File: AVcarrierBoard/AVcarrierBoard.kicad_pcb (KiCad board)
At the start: 4 copper layers, 253.6 x 59 mm, 18 parts, among them J1 Mech_Switch, J2 Mech_Switch, J3 MainRecov, J4 DrogRecov, J5 Staging, J6 Mech_Switch, U2 WiFi Switch, U3 EggtimerQuantum, U4 EggfinderMini/FeatherGPS, U5 Blue_Raven

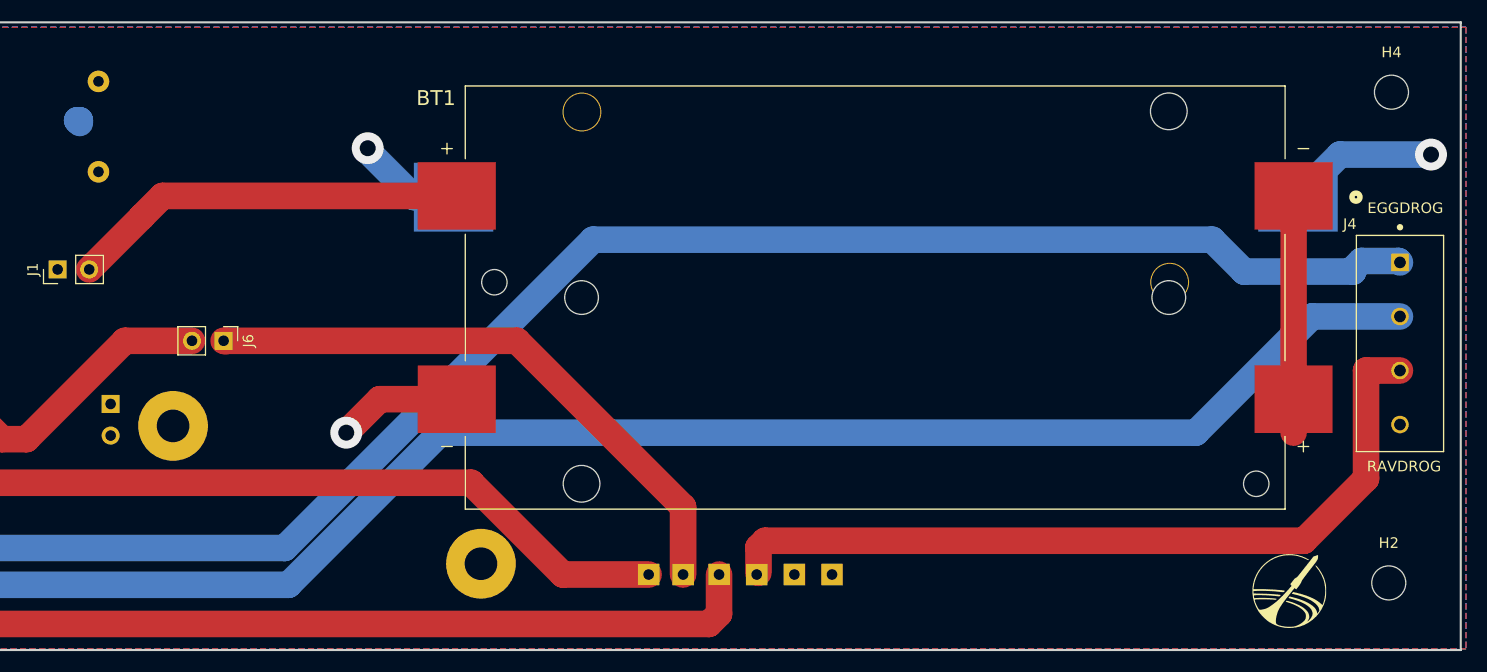
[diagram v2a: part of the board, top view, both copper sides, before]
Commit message: Added mounting holes for battery holders
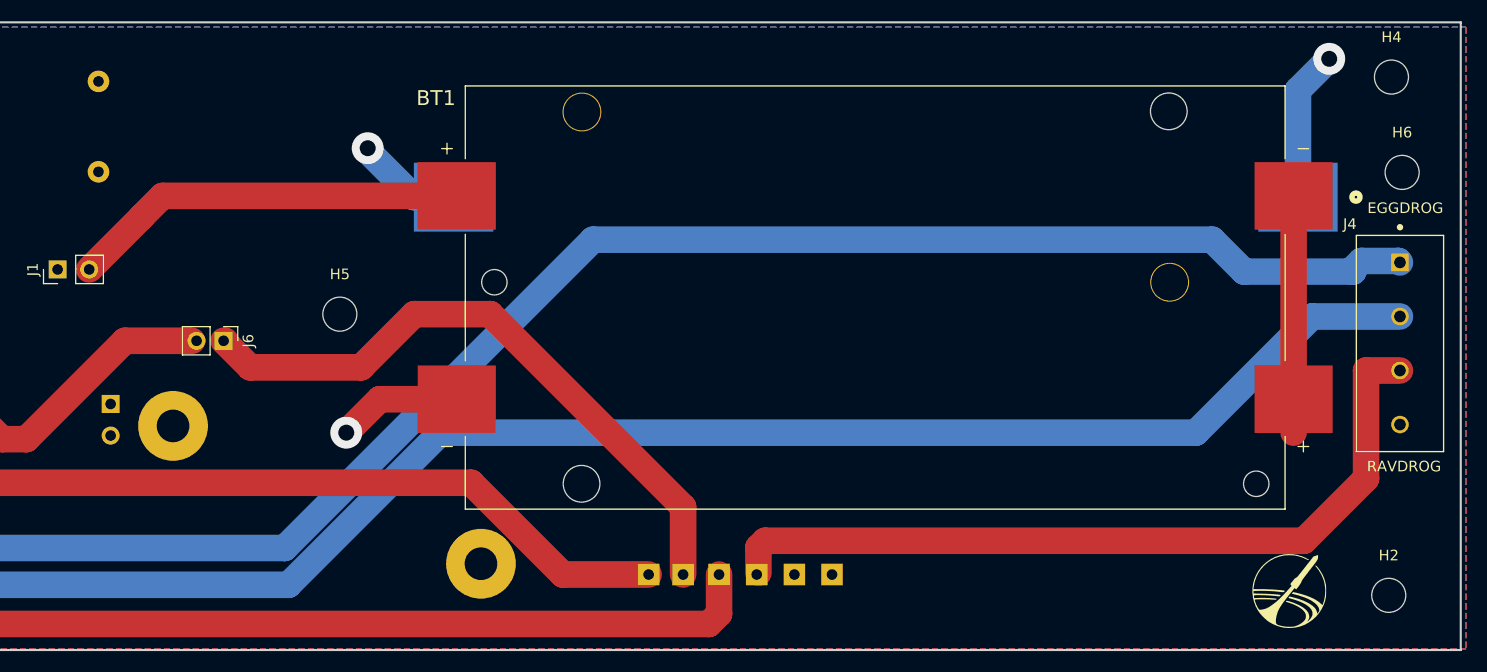
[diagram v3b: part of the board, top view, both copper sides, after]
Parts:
- added H5: M3, MountingHole:MountingHole_3.2mm_M3_ISO14580, F.Cu at (171.0, 93.0)
- added H6: M3, MountingHole:MountingHole_3.2mm_M3_ISO14580, F.Cu at (270.9, 79.7)
- J6: footprint 2.97mmSwitchConnector:PinHeader_1x02_P2.97mm_Vertical -> Connector_PinHeader_2.54mm:PinHeader_1x02_P2.54mm_Vertical
- moved H4 1.42 mm to (269.8, 70.7)
- moved H2 1.17 mm to (269.6, 119.4)
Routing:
- net +3V8: track 157.2 -> 151.4 mm
- net Raven3RD: track 56.1 -> 60.2 mm
- net GND2: track 10.9 -> 10.2 mm

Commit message: fix a bit
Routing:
- net +3V8: track 151.4 -> 129.8 mm
- net RavenMotIgnition: track 132.2 -> 124.5 mm
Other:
- board text added: "Phoenix 1.1"
- board text removed: "Phoenix 1.0"
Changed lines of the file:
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@@
   (gr_rect (start 22.765 65.57) (end 276.365 124.57)
     (stroke (width 0.2) (type default)) (fill none) (layer "Edge.Cuts"))
-  (gr_text "Phoenix 1.0\n" (at 265.7348 119.7864) (layer "B.SilkS")
+  (gr_text "Phoenix 1.1\n" (at 265.7348 119.7864) (layer "B.SilkS")
     (effects (font (size 3 3) (thickness 0.15)) (justify left bottom mirror))
   )
@@
     (effects (font (size 1 1) (thickness 0.15)) (justify right bottom))
   )
-  (via (at 264 69) (size 3) (drill 1.5) (layers "F.Cu" "B.Cu") (free) (net 1))
-  (segment (start 149.4536 104.4126) (end 149.4536 106.4768) (width 2.5) (layer "In1.Cu") (net 1))
-  (segment (start 149.4536 106.4768) (end 155.4988 112.522) (width 2.5) (layer "In1.Cu") (net 1))
-  (segment (start 219.9132 104.14) (end 243.2812 80.772) (width 2.5) (layer "In1.Cu") (net 1))
-  (segment (start 263 69) (end 264 69) (width 2.5) (layer "In1.Cu") (net 1))
-  (segment (start 155.4988 112.522) (end 171.958 112.522) (width 2.5) (layer "In1.Cu") (net 1))
-  (segment (start 243.2812 80.772) (end 251.228 80.772) (width 2.5) (layer "In1.Cu") (net 1))
-  (segment (start 251.228 80.772) (end 263 69) (width 2.5) (layer "In1.Cu") (net 1))
-  (segment (start 171.958 112.522) (end 180.34 104.14) (width 2.5) (layer "In1.Cu") (net 1))
-  (segment (start 180.34 104.14) (end 219.9132 104.14) (width 2.5) (layer "In1.Cu") (net 1))
-  (segment (start 261.065 81.999) (end 261.065 71.935) (width 2.5) (layer "B.Cu") (net 1))
-  (segment (start 261.065 71.935) (end 264 69) (width 2.5) (layer "B.Cu") (net 1))
+  (via (at 251.228 80.772) (size 3) (drill 1.5) (layers "F.Cu" "B.Cu") (free) (net 1))
+  (segment (start 155.4988 112.522) (end 149.4536 106.4768) (width 2.5) (layer "In1.Cu") (net 1))
+  (segment (start 171.958 112.522) (end 155.4988 112.522) (width 2.5) (layer "In1.Cu") (net 1))
+  (segment (start 243.2812 80.772) (end 219.9132 104.14) (width 2.5) (layer "In1.Cu") (net 1))
+  (segment (start 251.228 80.772) (end 243.2812 80.772) (width 2.5) (layer "In1.Cu") (net 1))
+  (segment (start 180.34 104.14) (end 171.958 112.522) (width 2.5) (layer "In1.Cu") (net 1))
+  (segment (start 219.9132 104.14) (end 180.34 104.14) (width 2.5) (layer "In1.Cu") (net 1))
+  (segment (start 149.4536 106.4768) (end 149.4536 104.4126) (width 2.5) (layer "In1.Cu") (net 1))
+  (segment (start 251.228 80.772) (end 259.838 80.772) (width 2.5) (layer "B.Cu") (net 1))
+  (segment (start 259.838 80.772) (end 261.065 81.999) (width 2.5) (layer "B.Cu") (net 1))
   (segment (start 174.7474 100.995) (end 181.99 100.995) (width 2.5) (layer "F.Cu") (net 2))
   (segment (start 172.2074 103.535) (end 174.7474 100.995) (width 2.5) (layer "F.Cu") (net 2))
@@
   (segment (start 182 82) (end 177.9614 82) (width 2.5) (layer "B.Cu") (net 14))
   (segment (start 177.9614 82) (end 173.618 77.6566) (width 2.5) (layer "B.Cu") (net 14))
-  (segment (start 150.7922 95.504) (end 157.1008 95.504) (width 2.5) (layer "F.Cu") (net 15))
-  (segment (start 141.5466 104.7496) (end 150.7922 95.504) (width 2.5) (layer "F.Cu") (net 15))
-  (segment (start 139.2428 104.7496) (end 141.5466 104.7496) (width 2.5) (layer "F.Cu") (net 15))
-  (segment (start 127.2032 92.71) (end 139.2428 104.7496) (width 2.5) (layer "F.Cu") (net 15))
+  (segment (start 127.2032 92.71) (end 129.9972 95.504) (width 2.5) (layer "F.Cu") (net 15))
+  (segment (start 129.9972 95.504) (end 157.1008 95.504) (width 2.5) (layer "F.Cu") (net 15))
   (via (at 127.2032 92.71) (size 3) (drill 2) (layers "F.Cu" "B.Cu") (net 15))
   (segment (start 43.557799 86.130432) (end 39.3578 81.930433) (width 2.5) (layer "B.Cu") (net 15))

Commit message: changes to blue raven orientation, radio power, wifi gnd, etc.
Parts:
- J1, J2: footprint 2.97mmSwitchConnector:PinHeader_1x02_P2.97mm_Vertical -> COTS_Boards:CON_436500227_MOL
- J6: footprint Connector_PinHeader_2.54mm:PinHeader_1x02_P2.54mm_Vertical -> COTS_Boards:CON_436500227_MOL
- moved U5 50.0 mm to (198.2, 101.3), turned to 180 degrees
- moved J6 24.6 mm to (156.2, 71.2), turned to 180 degrees
- moved J2 21.5 mm to (156.5, 81.1)
- moved J1 15.1 mm to (159.4, 91.4), turned to 0 degrees
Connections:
- U2 pad 2: GND2 -> GND3
- U4 pad 1: PWR_2S -> WIFI_PWR_1S
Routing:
- net PWR_2S: track 0.00 -> 134.8 mm
- net RavenAPO: track 75.5 -> 137.6 mm
- net Raven4TH: track 182.0 -> 130.3 mm
- net RavenMAIN: track 187.6 -> 140.0 mm
- net +3V8: track 129.8 -> 106.8 mm
- net Raven3RD: track 60.2 -> 75.8 mm
- net RavenMotIgnition: track 124.5 -> 137.8 mm
- net +7.5V: track 37.4 -> 30.4 mm
- net DROG2: track 163.8 -> 167.1 mm
- added copper zone on F.Cu, net GND
